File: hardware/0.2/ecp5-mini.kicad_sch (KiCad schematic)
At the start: 22 parts, among them J3 S7 Mini, J4 S7 Mini, U1 ECP5U_12_CABGA256, X1 DSC6101CI2A-016.0000

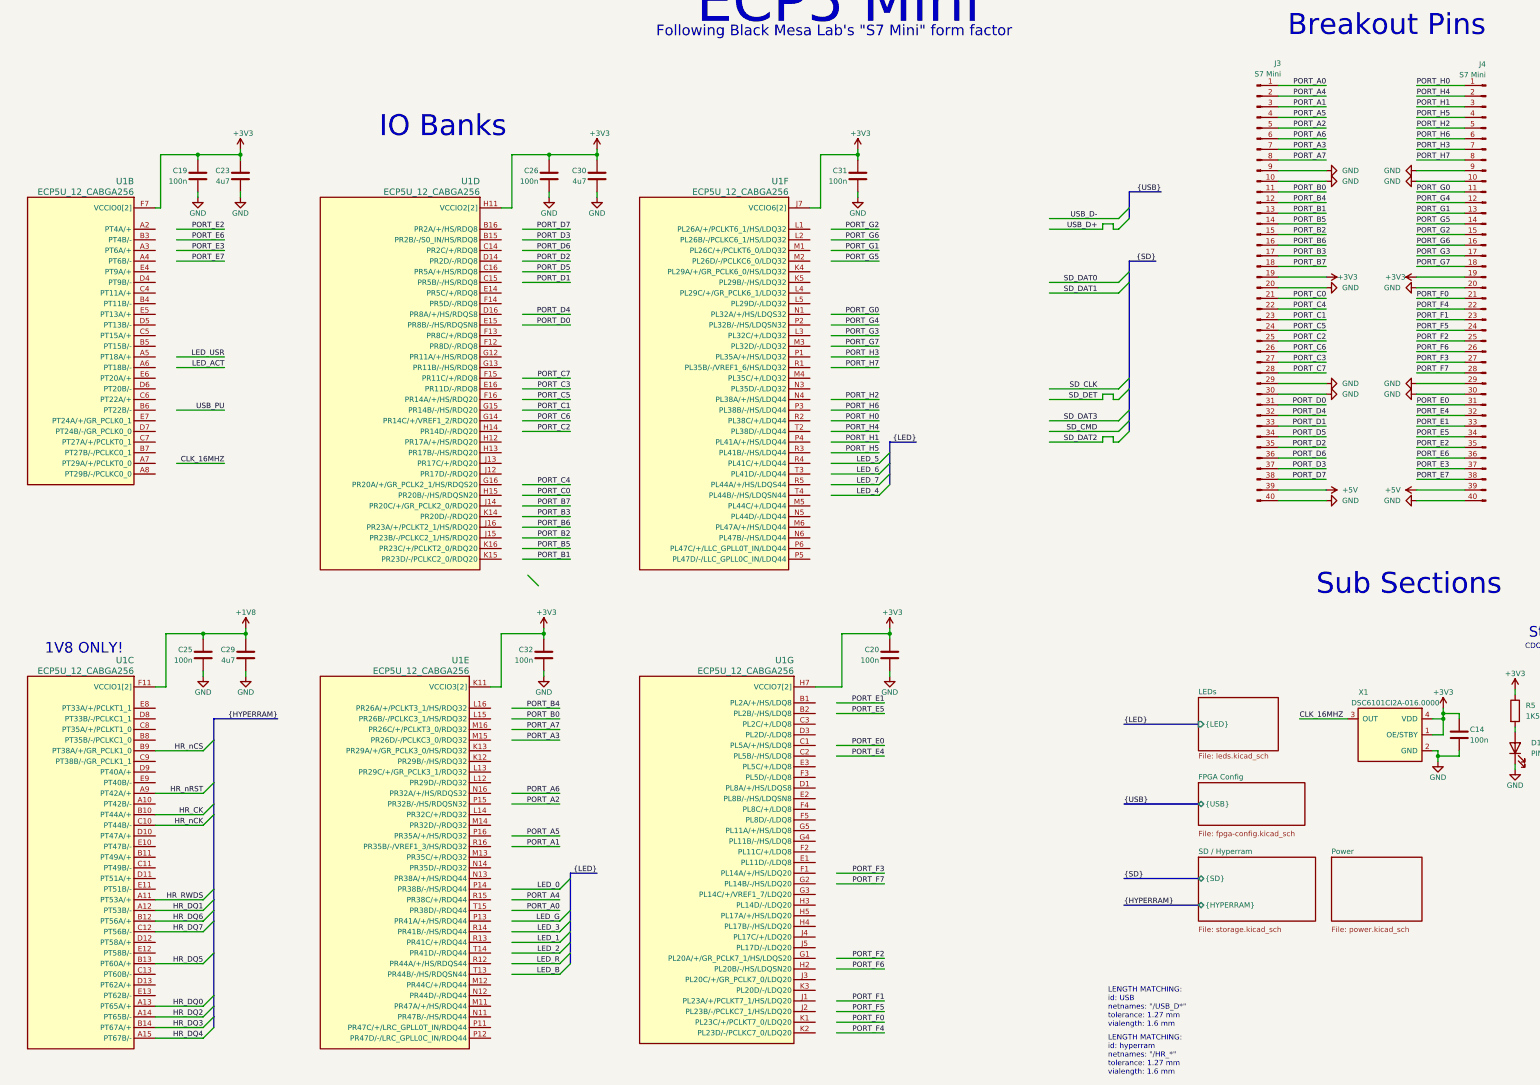
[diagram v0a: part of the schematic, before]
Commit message: half IO routed out
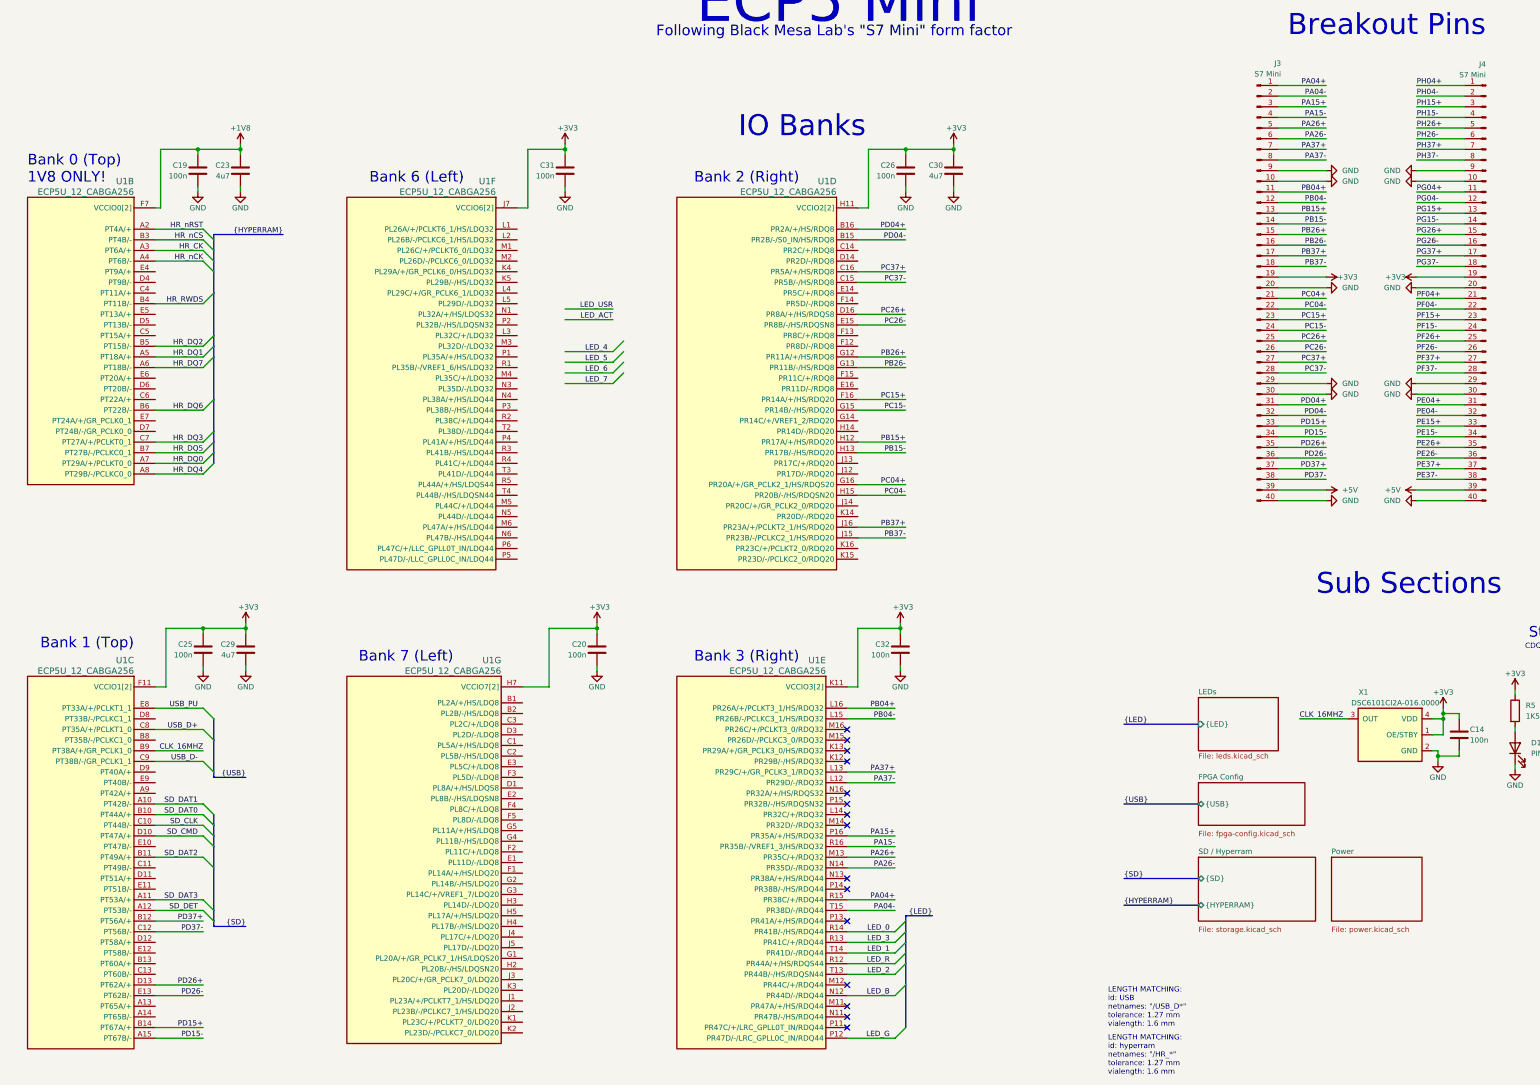
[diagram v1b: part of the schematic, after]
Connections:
- net PORT_A0 is gone; now on net PA04+: J3.1 (Pin_1)
- net PORT_A1 is gone; now on net PA15+: J3.3 (Pin_3)
- net PORT_A2 is gone; now on net PA26+: J3.5 (Pin_5)
- net PORT_A3 is gone; now on net PA37+: J3.7 (Pin_7)
- net PORT_A4 is gone; now on net PA04-: J3.2 (Pin_2)
- net PORT_A5 is gone; now on net PA15-: J3.4 (Pin_4)
- net PORT_A6 is gone; now on net PA26-: J3.6 (Pin_6)
- net PORT_A7 is gone; now on net PA37-: J3.8 (Pin_8)
- net PORT_B0 is gone; now on net PB04+: J3.11 (Pin_11)
- net PORT_B1 is gone; now on net PB15+: J3.13 (Pin_13)
- net PORT_B2 is gone; now on net PB26+: J3.15 (Pin_15)
- net PORT_B3 is gone; now on net PB37+: J3.17 (Pin_17)
- net PORT_B4 is gone; now on net PB04-: J3.12 (Pin_12)
- net PORT_B5 is gone; now on net PB15-: J3.14 (Pin_14)
- net PORT_B6 is gone; now on net PB26-: J3.16 (Pin_16)
- net PORT_B7 is gone; now on net PB37-: J3.18 (Pin_18)
- net PORT_C0 is gone; now on net PC04+: J3.21 (Pin_21)
- net PORT_C1 is gone; now on net PC15+: J3.23 (Pin_23)
- net PORT_C2 is gone; now on net PC26+: J3.25 (Pin_25)
- net PORT_C3 is gone; now on net PC37+: J3.27 (Pin_27)
- net PORT_C4 is gone; now on net PC04-: J3.22 (Pin_22)
- net PORT_C5 is gone; now on net PC15-: J3.24 (Pin_24)
- net PORT_C6 is gone; now on net PC26-: J3.26 (Pin_26)
- net PORT_C7 is gone; now on net PC37-: J3.28 (Pin_28)
- net PORT_D0 is gone; now on net PD04+: J3.31 (Pin_31)
- net PORT_D2 is gone; now on net PD26+: J3.35 (Pin_35)
- net PORT_D4 is gone; now on net PD04-: J3.32 (Pin_32)
- net PORT_D6 is gone; now on net PD26-: J3.36 (Pin_36)
- net +1V8: now also C19.1, C23.1, U1.F6 (VCCIO0[2]), U1.F7 (VCCIO0[2]); no longer C25.1, C29.1, U1.F10 (VCCIO1[2]), U1.F11 (VCCIO1[2])
- net +3V3: now also C25.1, C29.1, U1.F10 (VCCIO1[2]), U1.F11 (VCCIO1[2]); no longer C19.1, C23.1, U1.F6 (VCCIO0[2]), U1.F7 (VCCIO0[2])
- net CLK_16MHZ: now also U1.B9 (PT38A/+/GR_PCLK1_0)
- net HR_CK: now also U1.A3 (PT6A/+); no longer U1.B10 (PT44A/+)
- net HR_DQ0: now also U1.A7 (PT29A/+/PCLKT0_0); no longer U1.A13 (PT65A/+)
- net HR_DQ1: now also U1.A5 (PT18A/+); no longer U1.A12 (PT53B/-)
- net HR_DQ2: now also U1.B5 (PT15B/-); no longer U1.A14 (PT65B/-)
- net HR_DQ3: now also U1.C7 (PT27A/+/PCLKT0_1); no longer U1.B14 (PT67A/+)
- net HR_DQ4: now also U1.A8 (PT29B/-/PCLKC0_0); no longer U1.A15 (PT67B/-)
- net HR_DQ5: now also U1.B7 (PT27B/-/PCLKC0_1); no longer U1.B13 (PT60A/+)
- net HR_DQ6: now also U1.B6 (PT22B/-); no longer U1.B12 (PT56A/+)
- net HR_DQ7: now also U1.A6 (PT18B/-); no longer U1.C12 (PT56B/-)
- net HR_RWDS: now also U1.B4 (PT11B/-); no longer U1.A11 (PT53A/+)
- net HR_nCK: now also U1.A4 (PT6B/-); no longer U1.C10 (PT44B/-)
- net HR_nCS: now also U1.B3 (PT4B/-); no longer U1.B9 (PT38A/+/GR_PCLK1_0)
- net HR_nRST: now also U1.A2 (PT4A/+); no longer U1.A9 (PT42A/+)
- net LED_0: now also U1.R14 (PR41B/-/HS/RDQ44)
- net LED_1: now also U1.T14 (PR41D/-/RDQ44)
- net LED_2: now also U1.T13 (PR44B/-/HS/RDQSN44)
- net LED_3: now also U1.R13 (PR41C/+/RDQ44)
- net LED_B: now also U1.N12 (PR44D/-/RDQ44)
- net LED_G: now also U1.P12 (PR47D/-/LRC_GPLL0C_IN/RDQ44)
- net LED_R: now also U1.R12 (PR44A/+/HS/RDQS44)
- net SD_CLK: now also U1.C10 (PT44B/-)
- net SD_CMD: now also U1.D10 (PT47A/+)
- net SD_DAT0: now also U1.B10 (PT44A/+)
- net SD_DAT1: now also U1.A10 (PT42B/-)
- net SD_DAT2: now also U1.B11 (PT49A/+)
- net SD_DAT3: now also U1.A11 (PT53A/+)
- net SD_DET: now also U1.A12 (PT53B/-)
- net USB_D+: now also U1.C8 (PT35A/+/PCLKT1_0)
- net USB_D-: now also U1.C9 (PT38B/-/GR_PCLK1_1)
- net USB_PU: now also U1.E8 (PT33A/+/PCLKT1_1)
- net PA37-: now reaches U1.L12 (PR29D/-/RDQ32)
- net PA37+: now reaches U1.L13 (PR29C/+/GR_PCLK3_1/RDQ32)
- net PB04-: now reaches U1.L15 (PR26B/-/PCLKC3_1/HS/RDQ32)
- net PB04+: now reaches U1.L16 (PR26A/+/PCLKT3_1/HS/RDQ32)
- net PA26+: now reaches U1.M13 (PR35C/+/RDQ32)
- net PA26-: now reaches U1.N14 (PR35D/-/RDQ32)
- net PA15+: now reaches U1.P16 (PR35A/+/HS/RDQ32)
- net PA04+: now reaches U1.R15 (PR38C/+/RDQ44)
- net PA15-: now reaches U1.R16 (PR35B/-/VREF1_3/HS/RDQ32)
- net PA04-: now reaches U1.T15 (PR38D/-/RDQ44)
- net PD26+: now reaches U1.D13 (PT62A/+)
- net PD26-: now reaches U1.E13 (PT62B/-)
- net PD04-: now reaches U1.B15 (PR2B/-/S0_IN/HS/RDQ8)
- net PD04+: now reaches U1.B16 (PR2A/+/HS/RDQ8)
- net PC37-: now reaches U1.C15 (PR5B/-/HS/RDQ8)
- net PC37+: now reaches U1.C16 (PR5A/+/HS/RDQ8)
- net PC26+: now reaches U1.D16 (PR8A/+/HS/RDQS8)
- net PC26-: now reaches U1.E15 (PR8B/-/HS/RDQSN8)
- net PC15+: now reaches U1.F16 (PR14A/+/HS/RDQ20)
- net PB26+: now reaches U1.G12 (PR11A/+/HS/RDQ8)
- net PB26-: now reaches U1.G13 (PR11B/-/HS/RDQ8)
- net PC15-: now reaches U1.G15 (PR14B/-/HS/RDQ20)
- net PC04+: now reaches U1.G16 (PR20A/+/GR_PCLK2_1/HS/RDQS20)
- net PB15+: now reaches U1.H12 (PR17A/+/HS/RDQ20)
- net PB15-: now reaches U1.H13 (PR17B/-/HS/RDQ20)
- net PC04-: now reaches U1.H15 (PR20B/-/HS/RDQSN20)
- net PB37-: now reaches U1.J15 (PR23B/-/PCLKC2_1/HS/RDQ20)
- net PB37+: now reaches U1.J16 (PR23A/+/PCLKT2_1/HS/RDQ20)
- net PORT_D1 renamed PD15+
- net PD15+: now also U1.B14 (PT67A/+)
- net PORT_D3 renamed PD37+
- net PD37+: now also U1.B12 (PT56A/+)
- net PORT_D5 renamed PD15-
- net PD15-: now also U1.A15 (PT67B/-)
- net PORT_D7 renamed PD37-
- net PD37-: now also U1.C12 (PT56B/-)
- net PORT_E0 renamed PE04+
- net PORT_E1 renamed PE15+
- net PORT_E2 renamed PE26+
- net PORT_E3 renamed PE37+
- net PORT_E4 renamed PE04-
- net PORT_E5 renamed PE15-
- net PORT_E6 renamed PE26-
- net PORT_E7 renamed PE37-
- net PORT_F0 renamed PF04+
- net PORT_F1 renamed PF15+
- net PORT_F2 renamed PF26+
- net PORT_F3 renamed PF37+
- net PORT_F4 renamed PF04-
- net PORT_F5 renamed PF15-
- net PORT_F6 renamed PF26-
- net PORT_F7 renamed PF37-
- net PORT_G0 renamed PG04+
- net PORT_G1 renamed PG15+
- net PORT_G2 renamed PG26+
- net PORT_G3 renamed PG37+
- net PORT_G4 renamed PG04-
- net PORT_G5 renamed PG15-
- net PORT_G6 renamed PG26-
- net PORT_G7 renamed PG37-
- net PORT_H0 renamed PH04+
- net PORT_H1 renamed PH15+
- net PORT_H2 renamed PH26+
- net PORT_H3 renamed PH37+
- net PORT_H4 renamed PH04-
- net PORT_H5 renamed PH15-
- net PORT_H6 renamed PH26-
- net PORT_H7 renamed PH37-
- no-connect marks 0 -> 15
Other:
- note added: "Bank 0 (Top) 1V8 ONLY!"
- note added: "Bank 1 (Top)"
- note added: "Bank 2 (Right)"
- note added: "Bank 3 (Right)"
- note added: "Bank 6 (Left)"
- note added: "Bank 7 (Left)"
- note removed: "1V8 ONLY!"
- moved on the sheet: C19, C20, C23, C25, C26, C29, C30, C31, C32, U1D, U1E, U1F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
